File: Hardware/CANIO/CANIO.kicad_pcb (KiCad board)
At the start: 4 copper layers, 70 x 47.5 mm, 37 parts, among them J102 Tag Connect, J103 PWR, J201 CAN, J202 CAN, P101 USB_C_Plug_USB2.0, SW101 RESET, U101 ATmega16U2, U201 MCP25625-x-SS, Y101 DNP, Y202 Crystal_GND24

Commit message: Do some routing
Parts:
- added TP101: STBY, TestPoint:TestPoint_Pad_2.0x2.0mm, F.Cu at (2.75, -12.2)
- added TP102: TestPoint, TestPoint:TestPoint_Pad_2.0x2.0mm, B.Cu at (17.0, -20.2)
- added TP103: TestPoint, TestPoint:TestPoint_Pad_2.0x2.0mm, F.Cu at (21.5, -5.00)
- added TP104: TestPoint, TestPoint:TestPoint_Pad_2.0x2.0mm, F.Cu at (27.2, -2.00)
- added TP105: TestPoint, TestPoint:TestPoint_Pad_2.0x2.0mm, F.Cu at (24.2, -2.00)
- added TP106: TestPoint, TestPoint:TestPoint_Pad_2.0x2.0mm, B.Cu at (37.2, -32.2)
- added TP201: TestPoint, TestPoint:TestPoint_Pad_2.0x2.0mm, B.Cu at (7.75, -29.2)
- added TP202: TestPoint, TestPoint:TestPoint_Pad_2.0x2.0mm, B.Cu at (10.8, -29.2)
- added TP203: TestPoint, TestPoint:TestPoint_Pad_2.0x2.0mm, F.Cu at (18.8, -21.5)
- J102: moved to B.Cu
- moved J102 0.40 mm to (26.2, -8.37), turned to 180 degrees
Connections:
- R202 pad 2: /CANBUS/STBY -> /CAN_STBY
- U101 pad 14: unconnected-(U101-PB0-Pad14) -> /CS
- U101 pad 7: unconnected-(U101-PD1-Pad7) -> /CAN_STBY
- U101 pad 8: unconnected-(U101-PD2-Pad8) -> /CAN_INT
- U201 pad 13: /CANBUS/INT -> /CAN_INT
- U201 pad 17: /CANBUS/CS -> /CS
- U201 pad 5: /CANBUS/STBY -> /CAN_STBY
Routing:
- net /ICSP_RST: track 0.00 -> 44.6 mm
- net /ICSP_SCK: track 0.00 -> 40.4 mm, vias 0 -> 1
- net /ICSP_MOSI: track 0.00 -> 38.9 mm, vias 0 -> 4
- net /ICSP_MISO: track 0.00 -> 38.8 mm, vias 0 -> 3
- net /CS: track 0.00 -> 17.8 mm, vias 0 -> 1
- net /CLKOUT: track 0.00 -> 12.1 mm
- net /XTAL1: track 0.00 -> 11.0 mm, vias 0 -> 1
- net +5V: track 132.9 -> 142.0 mm, vias 8 -> 9
- net GND: track 12.3 -> 13.0 mm, vias 21 -> 22
- net Net-(JP101-A): track 0.00 -> 0.07 mm, vias 0 -> 1

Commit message: Everything seems ship shape
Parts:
- added D201: ACT, LED_SMD:LED_0805_2012Metric, F.Cu at (7.75, -39.8)
- added D202: DNP, LED_SMD:LED_0805_2012Metric, F.Cu at (10.8, -39.8)
- added R203: 1K, Resistor_SMD:R_0805_2012Metric, F.Cu at (7.75, -36.2)
- added R204: DNP, Resistor_SMD:R_0805_2012Metric, F.Cu at (10.8, -36.2)
- moved TP101 26.6 mm to (17.0, -34.8), turned to 180 degrees
- moved R202 21.3 mm to (16.7, -31.7), turned to 180 degrees
- moved R107 7.08 mm to (21.8, -20.8), turned to -90 degrees
- moved TP201 3.50 mm to (7.75, -32.8)
- moved TP202 3.50 mm to (10.8, -32.8)
- turned D102 to -90 degrees
- turned Y202 to -90 degrees
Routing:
- net /CAN_STBY: track 0.00 -> 34.2 mm
- net /CAN_INT: track 0.00 -> 32.7 mm
- net /CANBUS/CANH: track 0.00 -> 30.5 mm
- net +5V: track 142.0 -> 170.1 mm, vias 9 -> 10
- net /CANBUS/CANL: track 0.00 -> 23.3 mm
- net Net-(U201-RXD): track 0.00 -> 20.3 mm, vias 0 -> 3
- net Net-(U201-TXD): track 0.00 -> 18.9 mm, vias 0 -> 4
- net Net-(U101-D+): track 0.00 -> 16.4 mm, vias 0 -> 2
- net Net-(U101-D-): track 0.00 -> 16.0 mm, vias 0 -> 2
- net /XTAL2: track 0.00 -> 15.2 mm, vias 0 -> 2
- net /XTAL1: track 11.0 -> 25.1 mm, vias 1 -> 2
- net /CANBUS/XTAL2: track 0.00 -> 9.55 mm
- net GND: track 13.0 -> 22.0 mm, vias 22 -> 24
- net Net-(P101-CC): track 0.00 -> 7.78 mm
- net Net-(P101-VCONN): track 0.00 -> 7.29 mm
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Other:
- board text added: "If terminated do not use"
- board text added: "RX"
- board text added: "STAT"
- board text added: "TX"

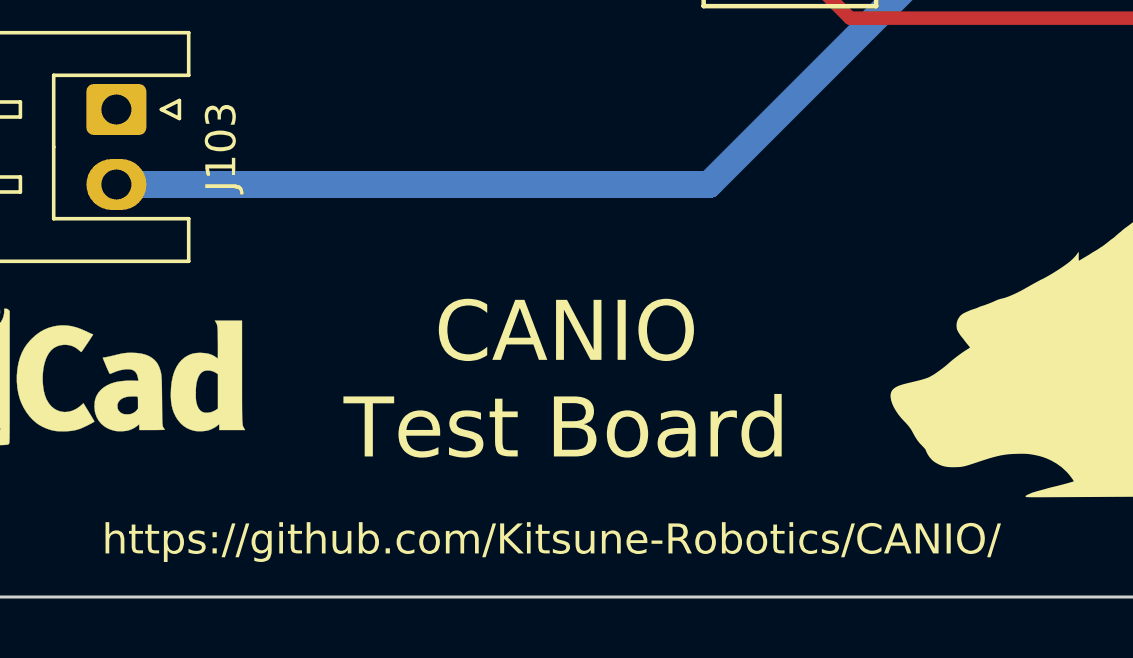
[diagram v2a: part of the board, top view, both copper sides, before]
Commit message: Add revision to silkscreen
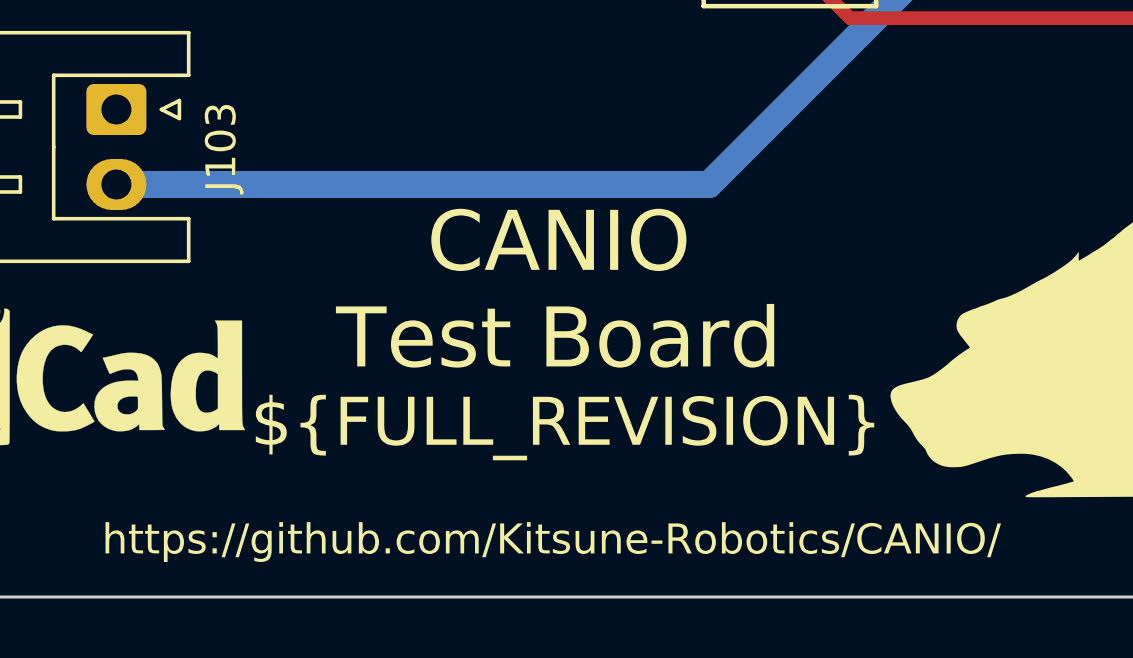
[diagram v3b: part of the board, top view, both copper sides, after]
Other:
- board text added: "${FULL_REVISION}"
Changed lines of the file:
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@@
     (effects (font (size 1.5 1.5) (thickness 0.3) bold) (justify left bottom))
   )
-  (gr_text "CANIO\nTest Board" (at -0.5 -7.5) (layer "F.SilkS")
+  (gr_text "CANIO\nTest Board" (at -0.75 -10.5) (layer "F.SilkS")
     (effects (font (size 2 2) (thickness 0.3)) (justify top))
   )
@@
     (effects (font (size 1.5 1.5) (thickness 0.3) bold) (justify left bottom))
   )
+  (gr_text "${FULL_REVISION}" (at -0.5 -4.25) (layer "F.SilkS")
+    (effects (font (size 1.6 1.6) (thickness 0.3)) (justify top))
+  )
   (segment (start 0.55 -19.05) (end 0.5 -19) (width 0.45) (layer "F.Cu") (net 1))

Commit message: Add a few more comments
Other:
- board text added: "Stencil Size is 90x65"
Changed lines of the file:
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@@
       (stroke (width 0) (type solid)) (fill solid) (layer "B.SilkS"))
   )
+  (gr_rect (start -35 -55) (end 55 10)
+    (stroke (width 0.15) (type default)) (fill none) (layer "Dwgs.User"))
   (gr_arc (start -22.5 2.5) (mid -24.267767 1.767767) (end -25 0)
     (stroke (width 0.1) (type default)) (layer "Edge.Cuts"))
@@
     (effects (font (size 1.6 1.6) (thickness 0.3)) (justify top))
   )
+  (gr_text "Stencil Size is 90x65" (at 10 -65) (layer "Dwgs.User")
+    (effects (font (size 3 3) (thickness 0.75) bold) (justify bottom))
+  )
+  (dimension (type aligned) (layer "Dwgs.User")
+    (pts (xy 55 -55) (xy -35 -55))
+    (height 5)
+    (gr_text "90.0000 mm" (at 10 -61.15) (layer "Dwgs.User")
+      (effects (font (size 1 1) (thickness 0.15)))
+    )
+    (format (prefix "") (suffix "") (units 3) (units_format 1) (precision 4))
+    (style (thickness 0.15) (arrow_length 1.27) (text_position_mode 0) (extension_height 0.58642) (extension_offset 0.5) keep_text_aligned)
+  )
+  (dimension (type aligned) (layer "Dwgs.User")
+    (pts (xy -35 -55) (xy -35 10))
+    (height 4.999999)
+    (gr_text "65.0000 mm" (at -41.149999 -22.5 90) (layer "Dwgs.User")
+      (effects (font (size 1 1) (thickness 0.15)))
+    )
+    (format (prefix "") (suffix "") (units 3) (units_format 1) (precision 4))
+    (style (thickness 0.15) (arrow_length 1.27) (text_position_mode 0) (extension_height 0.58642) (extension_offset 0.5) keep_text_aligned)
+  )
   (segment (start 0.55 -19.05) (end 0.5 -19) (width 0.45) (layer "F.Cu") (net 1))

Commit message: include input from @ka2qfx
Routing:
- net +5V: track 170.1 -> 165.4 mm
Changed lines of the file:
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@@
   (segment (start 28.226686 -12.79245) (end 27.448392 -12.014156) (width 0.45) (layer "B.Cu") (net 2))
   (segment (start 35.5 -23.95) (end 35.5 -30.245) (width 0.9) (layer "B.Cu") (net 2))
-  (segment (start 14.3 -21.295) (end 19.05 -26.045) (width 0.9) (layer "B.Cu") (net 2))
+  (segment (start 9.175 -30.42) (end 13.55 -26.045) (width 0.45) (layer "B.Cu") (net 2))
   (segment (start 34.55 -23) (end 34.55 -12.045) (width 0.9) (layer "B.Cu") (net 2))
   (segment (start 29.75 -26.045) (end 31.3 -26.045) (width 0.45) (layer "B.Cu") (net 2))
@@
   (segment (start 34.8 -11.795) (end 33.80255 -12.79245) (width 0.45) (layer "B.Cu") (net 2))
   (segment (start 31.3 -26.045) (end 27.5 -26.045) (width 0.9) (layer "B.Cu") (net 2))
-  (segment (start 11.75 -40.75) (end 26.455 -26.045) (width 0.45) (layer "B.Cu") (net 2))
+  (segment (start 11.75 -40.75) (end 9.175 -38.175) (width 0.45) (layer "B.Cu") (net 2))
+  (segment (start 15.55 -22.545) (end 15.55 -26.045) (width 0.9) (layer "B.Cu") (net 2))
+  (segment (start 9.175 -38.175) (end 9.175 -30.42) (width 0.45) (layer "B.Cu") (net 2))
   (segment (start 34.55 -12.045) (end 34.8 -11.795) (width 0.9) (layer "B.Cu") (net 2))
   (segment (start 15.55 -26.045) (end 13.3 -26.045) (width 0.9) (layer "B.Cu") (net 2))
@@
   (segment (start 27.5 -26.045) (end 19.55 -26.045) (width 0.9) (layer "B.Cu") (net 2))
   (segment (start 4.255 -11.25) (end 14.3 -21.295) (width 0.9) (layer "B.Cu") (net 2))
+  (segment (start 15.5025 -22.4975) (end 15.55 -22.545) (width 0.9) (layer "B.Cu") (net 2))
   (segment (start 13.3 -26.045) (end 9 -30.345) (width 0.9) (layer "B.Cu") (net 2))
   (segment (start 4.1 -30.345) (end 3.05 -29.295) (width 0.9) (layer "B.Cu") (net 2))
@@
   (segment (start 26.77 -7) (end 27.5 -7.73) (width 0.45) (layer "B.Cu") (net 2))
   (segment (start 19.05 -26.045) (end 19.55 -26.045) (width 0.9) (layer "B.Cu") (net 2))
+  (segment (start 14.3 -21.295) (end 15.5025 -22.4975) (width 0.9) (layer "B.Cu") (net 2))
   (segment (start 34.55 -29.295) (end 31.3 -26.045) (width 0.9) (layer "B.Cu") (net 2))
   (segment (start -7.75 -37.22) (end -2.5 -31.97) (width 0.9) (layer "F.Cu") (net 3))

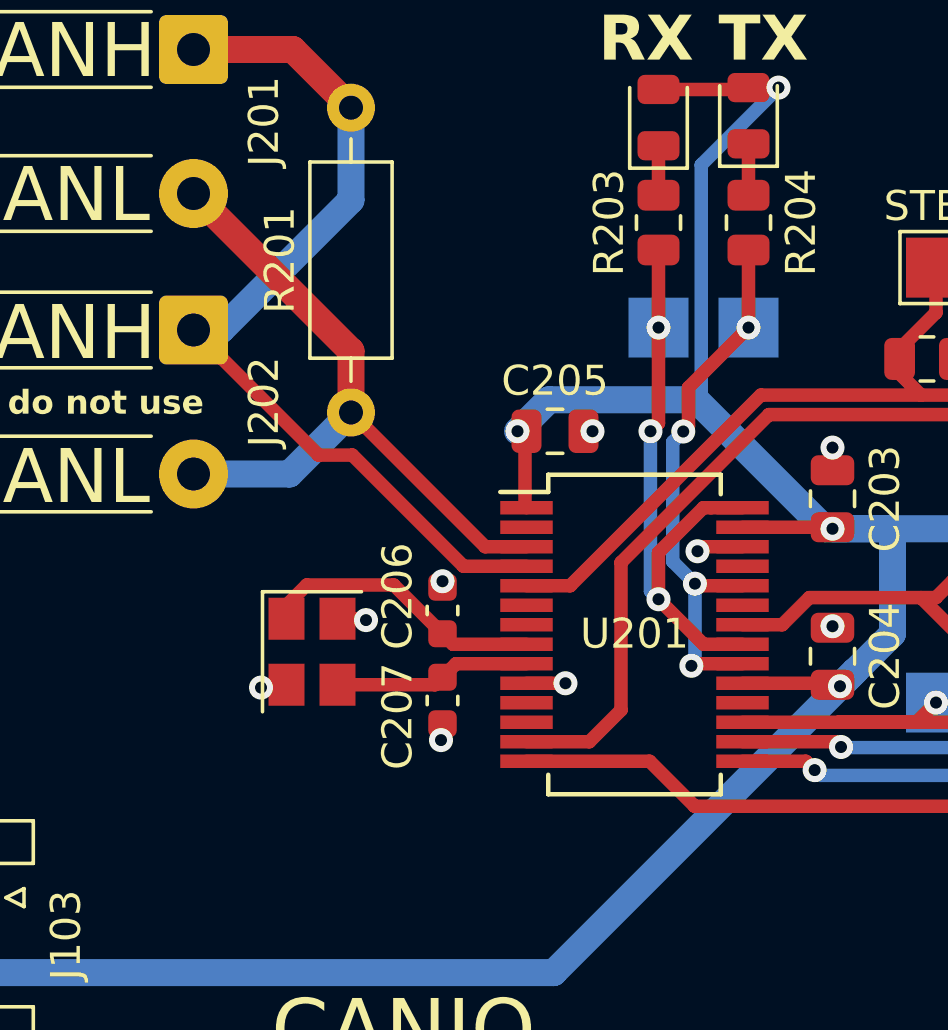
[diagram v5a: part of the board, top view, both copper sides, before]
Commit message: Add term solder jumper
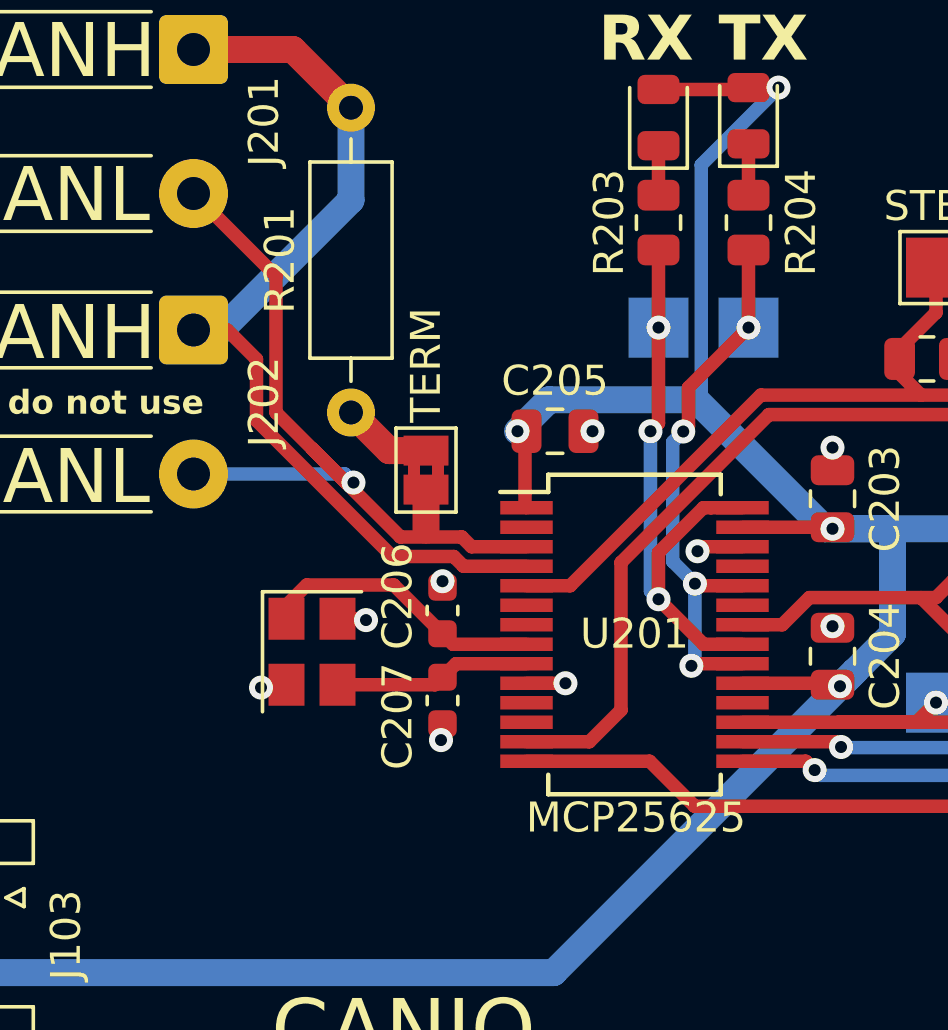
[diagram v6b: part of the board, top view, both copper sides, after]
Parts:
- added JP201: TERM, Jumper:SolderJumper-2_P1.3mm_Bridged2Bar_Pad1.0x1.5mm, F.Cu at (0.00, -28.0)
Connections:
- R201 pad 1: /CANBUS/CANL -> Net-(JP201-A)
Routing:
- net /CANBUS/CANL: track 23.3 -> 27.3 mm, vias 0 -> 1
- net Net-(JP201-A): track 0.00 -> 3.03 mm
- net /CANBUS/CANH: track 30.5 -> 31.7 mm
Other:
- board text added: "MCP25625"
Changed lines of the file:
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@@
   (net 56 "Net-(D201-K)")
   (net 57 "Net-(D202-K)")
+  (net 58 "Net-(JP201-A)")
   (footprint "Capacitor_SMD:C_0805_2012Metric" (layer "F.Cu")
     (at 4.3 -29.295)
@@
     )
   )
+  (footprint "Jumper:SolderJumper-2_P1.3mm_Bridged2Bar_Pad1.0x1.5mm" (layer "F.Cu")
+    (at 0 -28 -90)
+    (descr "SMD Solder Jumper, 1x1.5mm Pads, 0.3mm gap, bridged with 2 copper strips")
+    (tags "net tie solder jumper bridged")
+    (property "Sheetfile" "canbus.kicad_sch")
+    (property "Sheetname" "CANBUS")
+    (property "ki_description" "Solder Jumper, 2-pole, closed/bridged")
+    (property "ki_keywords" "solder jumper SPST")
+    (attr exclude_from_pos_files)
+    (net_tie_pad_groups "1, 2")
+    (fp_text reference "JP201" (at 0 -1.8 90) (layer "F.SilkS") hide
+        (effects (font (size 1 1) (thickness 0.15)))
+    )
+    (fp_text value "TERM" (at -3.5 0 90) (layer "F.SilkS")
+        (effects (font (size 1 1) (thickness 0.15)))
+    )
+    (fp_poly
+      (pts
+        (xy -0.25 -0.6)
+        (xy 0.25 -0.6)
+        (xy 0.25 -0.2)
+        (xy -0.25 -0.2)
+      )
+      (stroke (width 0) (type solid)) (fill solid) (layer "F.Cu"))
+    (fp_poly
+      (pts
+        (xy -0.25 0.2)
+        (xy 0.25 0.2)
+        (xy 0.25 0.6)
+        (xy -0.25 0.6)
+      )
+      (stroke (width 0) (type solid)) (fill solid) (layer "F.Cu"))
+    (fp_line (start -1.4 -1) (end 1.4 -1)
+      (stroke (width 0.12) (type solid)) (layer "F.SilkS"))
+    (fp_line (start -1.4 1) (end -1.4 -1)
+      (stroke (width 0.12) (type solid)) (layer "F.SilkS"))
+    (fp_line (start 1.4 -1) (end 1.4 1)
+      (stroke (width 0.12) (type solid)) (layer "F.SilkS"))
+    (fp_line (start 1.4 1) (end -1.4 1)
+      (stroke (width 0.12) (type solid)) (layer "F.SilkS"))
+    (fp_line (start -1.65 -1.25) (end -1.65 1.25)
+      (stroke (width 0.05) (type solid)) (layer "F.CrtYd"))
+    (fp_line (start -1.65 -1.25) (end 1.65 -1.25)
+      (stroke (width 0.05) (type solid)) (layer "F.CrtYd"))
+    (fp_line (start 1.65 1.25) (end -1.65 1.25)
+      (stroke (width 0.05) (type solid)) (layer "F.CrtYd"))
+    (fp_line (start 1.65 1.25) (end 1.65 -1.25)
+      (stroke (width 0.05) (type solid)) (layer "F.CrtYd"))
+    (pad "1" smd rect (at -0.65 0 270) (size 1 1.5) (layers "F.Cu" "F.Mask")
+      (net 58 "Net-(JP201-A)") (pinfunction "A") (pintype "passive"))
+    (pad "2" smd rect (at 0.65 0 270) (size 1 1.5) (layers "F.Cu" "F.Mask")
+      (net 3 "/CANBUS/CANL") (pinfunction "B") (pintype "passive"))
+  )
   (footprint "Resistor_SMD:R_0805_2012Metric" (layer "F.Cu")
     (at 40.05 -39.795 90)
@@
       (stroke (width 0.1) (type solid)) (layer "F.Fab"))
     (pad "1" thru_hole circle (at 0 0 90) (size 1.6 1.6) (drill 0.8) (layers "*.Cu" "*.Mask")
-      (net 3 "/CANBUS/CANL") (pintype "passive"))
+      (net 58 "Net-(JP201-A)") (pintype "passive"))
     (pad "2" thru_hole oval (at 10.16 0 90) (size 1.6 1.6) (drill 0.8) (layers "*.Cu" "*.Mask")
       (net 4 "/CANBUS/CANH") (pintype "passive"))
@@
     (effects (font (size 1.5 1.5) (thickness 0.3) bold) (justify left bottom))
   )
+  (gr_text "MCP25625\n" (at 7 -17) (layer "F.SilkS")
+    (effects (font (size 1 1) (thickness 0.15)) (justify top))
+  )
   (gr_text "CANL" (at -9.2 -27.77) (layer "F.SilkS" knockout)
     (effects (font (size 1.8 1.8) (thickness 0.25)) (justify right))
@@
   (segment (start 14.3 -21.295) (end 15.5025 -22.4975) (width 0.9) (layer "B.Cu") (net 2))
   (segment (start 34.55 -29.295) (end 31.3 -26.045) (width 0.9) (layer "B.Cu") (net 2))
-  (segment (start -7.75 -37.22) (end -2.5 -31.97) (width 0.9) (layer "F.Cu") (net 3))
-  (segment (start 3.35 -25.445) (end 1.975 -25.445) (width 0.45) (layer "F.Cu") (net 3))
-  (segment (start 1.975 -25.445) (end -2.5 -29.92) (width 0.45) (layer "F.Cu") (net 3))
-  (segment (start -2.5 -31.97) (end -2.5 -29.92) (width 0.9) (layer "F.Cu") (net 3))
-  (segment (start -4.55 -27.87) (end -2.5 -29.92) (width 0.9) (layer "B.Cu") (net 3))
-  (segment (start -7.75 -27.87) (end -4.55 -27.87) (width 0.9) (layer "B.Cu") (net 3))
+  (segment (start -5 -29.919238) (end -3.790381 -28.709619) (width 0.45) (layer "F.Cu") (net 3))
+  (segment (start -7.75 -37.22) (end -5 -34.47) (width 0.45) (layer "F.Cu") (net 3))
+  (segment (start -2.664126 -27.583364) (end -3.790381 -28.709619) (width 0.45) (layer "F.Cu") (net 3))
+  (segment (start 0 -27.35) (end 0 -25.995) (width 0.9) (layer "F.Cu") (net 3))
+  (segment (start -0.850762 -25.77) (end 1.194712 -25.77) (width 0.45) (layer "F.Cu") (net 3))
+  (segment (start 1.519712 -25.445) (end 3.35 -25.445) (width 0.45) (layer "F.Cu") (net 3))
+  (segment (start -2.416636 -27.583364) (end -2.664126 -27.583364) (width 0.45) (layer "F.Cu") (net 3))
+  (segment (start 1.194712 -25.77) (end 1.519712 -25.445) (width 0.45) (layer "F.Cu") (net 3))
+  (segment (start -3.790381 -28.709619) (end -0.850762 -25.77) (width 0.45) (layer "F.Cu") (net 3))
+  (segment (start -5 -34.47) (end -5 -29.919238) (width 0.45) (layer "F.Cu") (net 3))
+  (via (at -2.416636 -27.583364) (size 0.8) (drill 0.4) (layers "F.Cu" "B.Cu") (net 3))
+  (segment (start -2.703272 -27.87) (end -7.75 -27.87) (width 0.45) (layer "B.Cu") (net 3))
+  (segment (start -2.416636 -27.583364) (end -2.703272 -27.87) (width 0.45) (layer "B.Cu") (net 3))
   (segment (start -4.44 -42.02) (end -2.5 -40.08) (width 0.9) (layer "F.Cu") (net 4))
-  (segment (start 1.250474 -24.795) (end -2.454526 -28.5) (width 0.45) (layer "F.Cu") (net 4))
-  (segment (start -2.454526 -28.5) (end -3.58 -28.5) (width 0.45) (layer "F.Cu") (net 4))
-  (segment (start -3.58 -28.5) (end -7.75 -32.67) (width 0.45) (layer "F.Cu") (net 4))
+  (segment (start -5.65 -31.695474) (end -6.624526 -32.67) (width 0.45) (layer "F.Cu") (net 4))
+  (segment (start -5.65 -29.65) (end -5.65 -31.695474) (width 0.45) (layer "F.Cu") (net 4))
+  (segment (start -6.624526 -32.67) (end -7.75 -32.67) (width 0.45) (layer "F.Cu") (net 4))
+  (segment (start 0.925474 -25.12) (end -1.12 -25.12) (width 0.45) (layer "F.Cu") (net 4))
   (segment (start 3.35 -24.795) (end 1.250474 -24.795) (width 0.45) (layer "F.Cu") (net 4))
+  (segment (start -1.12 -25.12) (end -5.65 -29.65) (width 0.45) (layer "F.Cu") (net 4))
   (segment (start -7.75 -42.02) (end -4.44 -42.02) (width 0.9) (layer "F.Cu") (net 4))
+  (segment (start 1.250474 -24.795) (end 0.925474 -25.12) (width 0.45) (layer "F.Cu") (net 4))
   (segment (start -6.83 -32.67) (end -7.75 -32.67) (width 0.9) (layer "B.Cu") (net 4))
   (segment (start -2.5 -40.08) (end -2.5 -37) (width 0.9) (layer "B.Cu") (net 4))
@@
   (segment (start 10.75 -37.5) (end 10.5 -37.25) (width 0.45) (layer "F.Cu") (net 57))
   (segment (start 10.75 -38.625) (end 10.75 -37.5) (width 0.45) (layer "F.Cu") (net 57))
+  (segment (start -1.23 -28.65) (end -2.5 -29.92) (width 0.9) (layer "F.Cu") (net 58))
+  (segment (start 0 -28.65) (end -1.23 -28.65) (width 0.9) (layer "F.Cu") (net 58))
   (zone (net 1) (net_name "GND") (layer "In1.Cu") (hatch edge 0.5)
     (connect_pads (clearance 0.5))
